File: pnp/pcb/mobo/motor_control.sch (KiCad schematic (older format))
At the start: 43 parts, among them J1 X_MOTOR, J2 Y_MOTOR1, J3 Z_MOTOR, J37 P_MOTOR, J38 C_MOTOR, J4 R_MOTOR, J48 Y_MOTOR2

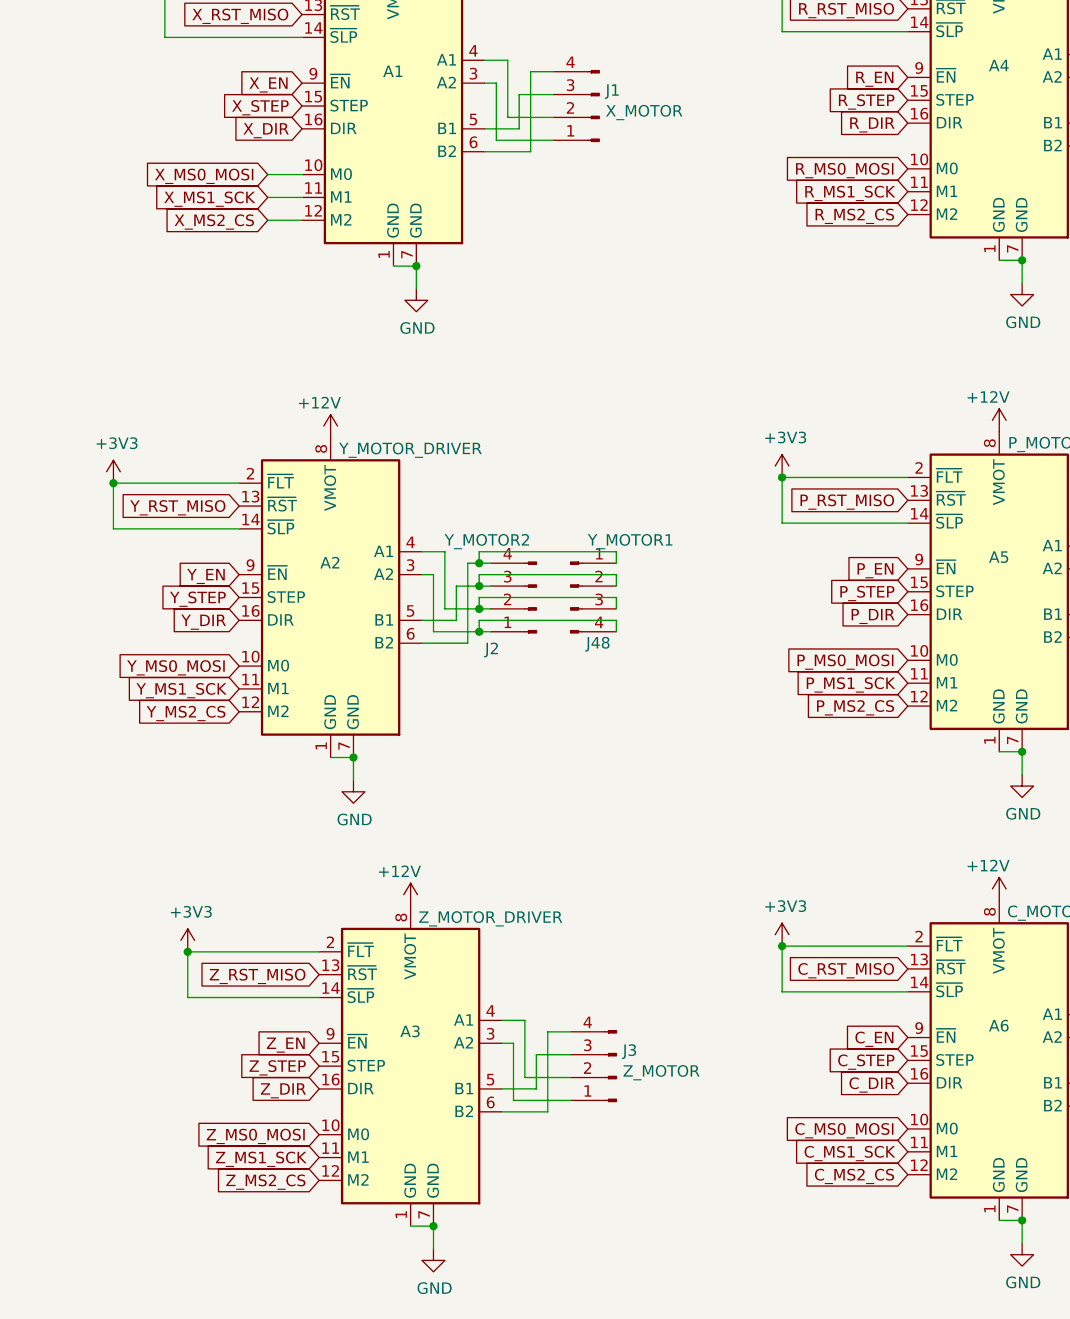
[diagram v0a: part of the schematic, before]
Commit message: Add support for Trinamic UART and SPI drivers
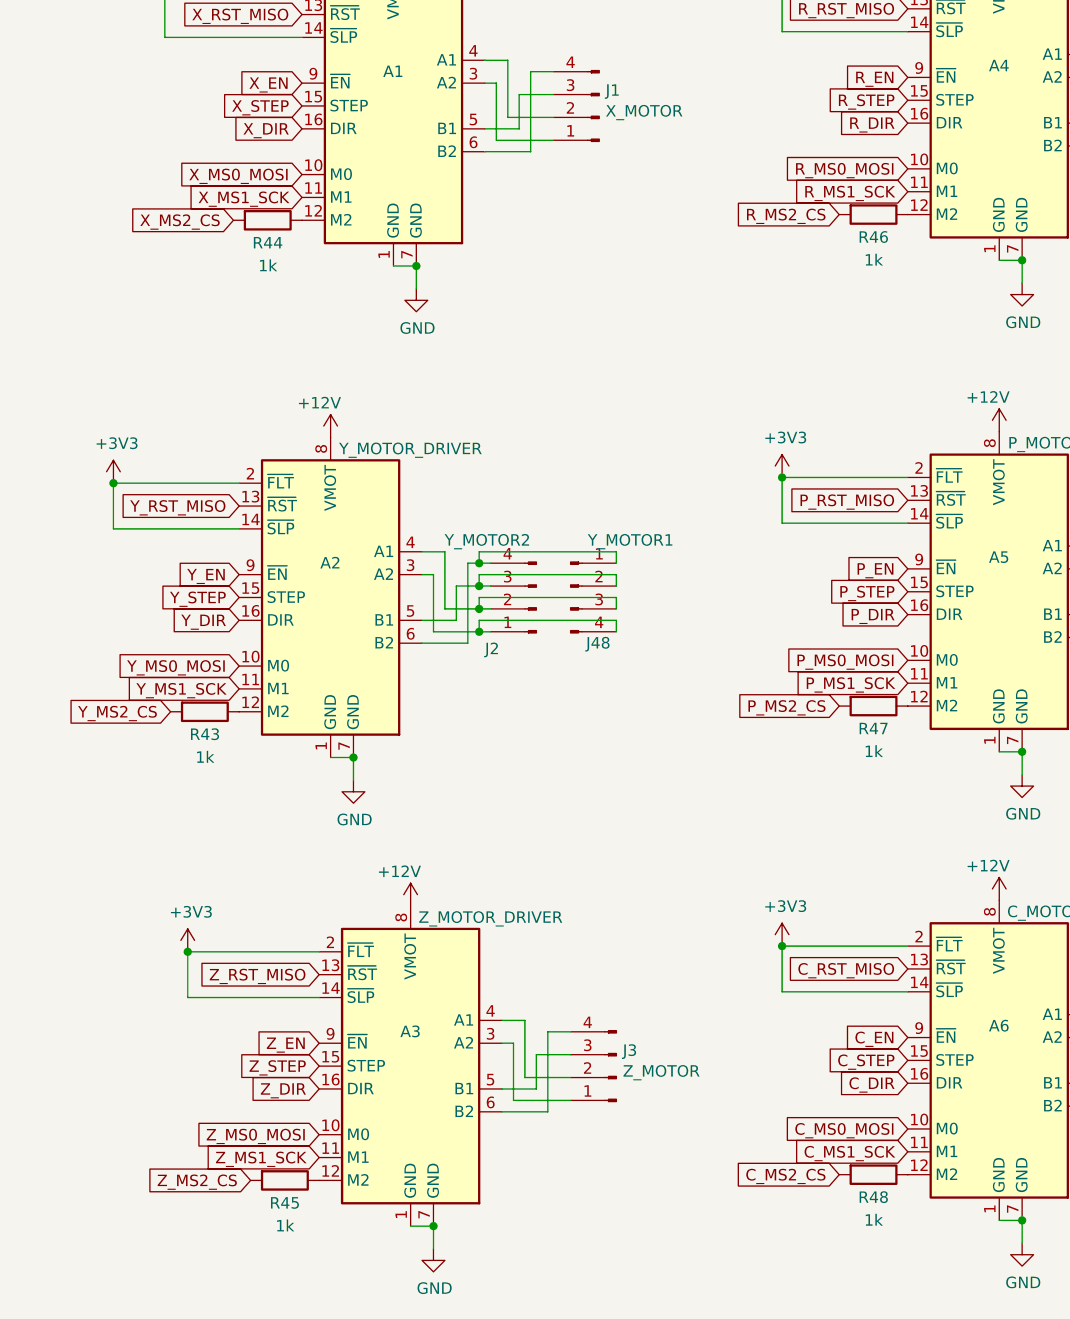
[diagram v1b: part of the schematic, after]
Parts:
- added R43, R44, R45, R46, R47, R48: 1k, Resistor_SMD:R_0805_2012Metric_Pad1.20x1.40mm_HandSolder, symbol Device:R
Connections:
- net C_MS2_CS: now also R48.2; no longer A6.12 (M2)
- net P_MS2_CS: now also R47.2; no longer A5.12 (M2)
- net R_MS2_CS: now also R46.2; no longer A4.12 (M2)
- net X_MS2_CS: now also R44.2; no longer A1.12 (M2)
- net Y_MS2_CS: now also R43.2; no longer A2.12 (M2)
- net Z_MS2_CS: now also R45.2; no longer A3.12 (M2)
- new net: A3.12 (M2), R45.1
- new net: A1.12 (M2), R44.1
- new net: A2.12 (M2), R43.1
- new net: A6.12 (M2), R48.1
- new net: A4.12 (M2), R46.1
- new net: A5.12 (M2), R47.1
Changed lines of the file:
@@
 Connection ~ 3050 1050
 Connection ~ 2650 1050
-Text GLabel 1825 2150 0    50   Input ~ 0
-X_EN
 Text GLabel 1825 2250 0    50   Input ~ 0
 X_STEP
@@
 Text GLabel 4475 2325 0    50   Input ~ 0
 R_DIR
-Text GLabel 1550 4300 0    50   Input ~ 0
-Y_EN
 Text GLabel 1550 4400 0    50   Input ~ 0
 Y_STEP
@@
 Text GLabel 4475 4475 0    50   Input ~ 0
 P_DIR
-Text GLabel 1900 6350 0    50   Input ~ 0
-Z_EN
 Text GLabel 1900 6450 0    50   Input ~ 0
 Z_STEP
@@
 Wire Wire Line
 	5275 2025 5375 2025
-Text GLabel 1675 2550 0    50   Input ~ 0
+Text GLabel 1825 2550 0    50   Input ~ 0
 X_MS0_MOSI
-Wire Wire Line
-	1675 2550 1825 2550
-Text GLabel 1675 2650 0    50   Input ~ 0
+Text GLabel 1825 2650 0    50   Input ~ 0
 X_MS1_SCK
-Text GLabel 1675 2750 0    50   Input ~ 0
+Text GLabel 1525 2750 0    50   Input ~ 0
 X_MS2_CS
 Text GLabel 1825 1850 0    50   Input ~ 0
@@
 	1225 1950 1825 1950
 Connection ~ 1225 1750
-Wire Wire Line
-	1675 2650 1825 2650
-Wire Wire Line
-	1675 2750 1825 2750
 Text GLabel 1550 4000 0    50   Input ~ 0
 Y_RST_MISO
@@
 Text GLabel 1550 4800 0    50   Input ~ 0
 Y_MS1_SCK
-Text GLabel 1550 4900 0    50   Input ~ 0
+Text GLabel 1250 4900 0    50   Input ~ 0
 Y_MS2_CS
 Wire Wire Line
@@
 Text GLabel 1900 6850 0    50   Input ~ 0
 Z_MS1_SCK
-Text GLabel 1900 6950 0    50   Input ~ 0
+Text GLabel 1600 6950 0    50   Input ~ 0
 Z_MS2_CS
 Text GLabel 4475 2525 0    50   Input ~ 0
@@
 Text GLabel 4475 2625 0    50   Input ~ 0
 R_MS1_SCK
-Text GLabel 4475 2725 0    50   Input ~ 0
+Text GLabel 4175 2725 0    50   Input ~ 0
 R_MS2_CS
 Text GLabel 4475 1825 0    50   Input ~ 0
@@
 Text GLabel 4475 4775 0    50   Input ~ 0
 P_MS1_SCK
-Text GLabel 4475 4875 0    50   Input ~ 0
+Text GLabel 4175 4875 0    50   Input ~ 0
 P_MS2_CS
 Text GLabel 4475 3975 0    50   Input ~ 0
@@
 Text GLabel 4475 6825 0    50   Input ~ 0
 C_MS1_SCK
-Text GLabel 4475 6925 0    50   Input ~ 0
+Text GLabel 4175 6925 0    50   Input ~ 0
 C_MS2_CS
 Text GLabel 4475 6025 0    50   Input ~ 0
@@
 	9300 1450 9300 1350
 Connection ~ 9300 1450
+Text GLabel 1825 2150 0    50   Input ~ 0
+X_EN
+Text GLabel 1900 6350 0    50   Input ~ 0
+Z_EN
+Text GLabel 1550 4300 0    50   Input ~ 0
+Y_EN
+$Comp
+L Device:R R47
+U 1 1 5FE64F8F
+P 4325 4875
+F 0 "R47" V 4425 4875 50  0000 C CNN
+F 1 "1k" V 4525 4875 50  0000 C CNN
+F 2 "Resistor_SMD:R_0805_2012Metric_Pad1.20x1.40mm_HandSolder" V 4255 4875 50  0001 C CNN
+F 3 "~" H 4325 4875 50  0001 C CNN
+	1    4325 4875
+	0    1    1    0
+$EndComp
+$Comp
+L Device:R R43
+U 1 1 5FE77D44
+P 1400 4900
+F 0 "R43" V 1500 4900 50  0000 C CNN
+F 1 "1k" V 1600 4900 50  0000 C CNN
+F 2 "Resistor_SMD:R_0805_2012Metric_Pad1.20x1.40mm_HandSolder" V 1330 4900 50  0001 C CNN
+F 3 "~" H 1400 4900 50  0001 C CNN
+	1    1400 4900
+	0    1    1    0
+$EndComp
+$Comp
+L Device:R R46
+U 1 1 5FE853A1
+P 4325 2725
+F 0 "R46" V 4425 2725 50  0000 C CNN
+F 1 "1k" V 4525 2725 50  0000 C CNN
+F 2 "Resistor_SMD:R_0805_2012Metric_Pad1.20x1.40mm_HandSolder" V 4255 2725 50  0001 C CNN
+F 3 "~" H 4325 2725 50  0001 C CNN
+	1    4325 2725
+	0    1    1    0
+$EndComp
+$Comp
+L Device:R R44
+U 1 1 5FE9EC8A
+P 1675 2750
+F 0 "R44" V 1775 2750 50  0000 C CNN
+F 1 "1k" V 1875 2750 50  0000 C CNN
+F 2 "Resistor_SMD:R_0805_2012Metric_Pad1.20x1.40mm_HandSolder" V 1605 2750 50  0001 C CNN
+F 3 "~" H 1675 2750 50  0001 C CNN
+	1    1675 2750
+	0    1    1    0
+$EndComp
+$Comp
+L Device:R R45
+U 1 1 5FEA6A5A
+P 1750 6950
+F 0 "R45" V 1850 6950 50  0000 C CNN
+F 1 "1k" V 1950 6950 50  0000 C CNN
+F 2 "Resistor_SMD:R_0805_2012Metric_Pad1.20x1.40mm_HandSolder" V 1680 6950 50  0001 C CNN
+F 3 "~" H 1750 6950 50  0001 C CNN
+	1    1750 6950
+	0    1    1    0
+$EndComp
+$Comp
+L Device:R R48
+U 1 1 5FEA9C63
+P 4325 6925
+F 0 "R48" V 4425 6925 50  0000 C CNN
+F 1 "1k" V 4525 6925 50  0000 C CNN
+F 2 "Resistor_SMD:R_0805_2012Metric_Pad1.20x1.40mm_HandSolder" V 4255 6925 50  0001 C CNN
+F 3 "~" H 4325 6925 50  0001 C CNN
+	1    4325 6925
+	0    1    1    0
+$EndComp
 $EndSCHEMATC

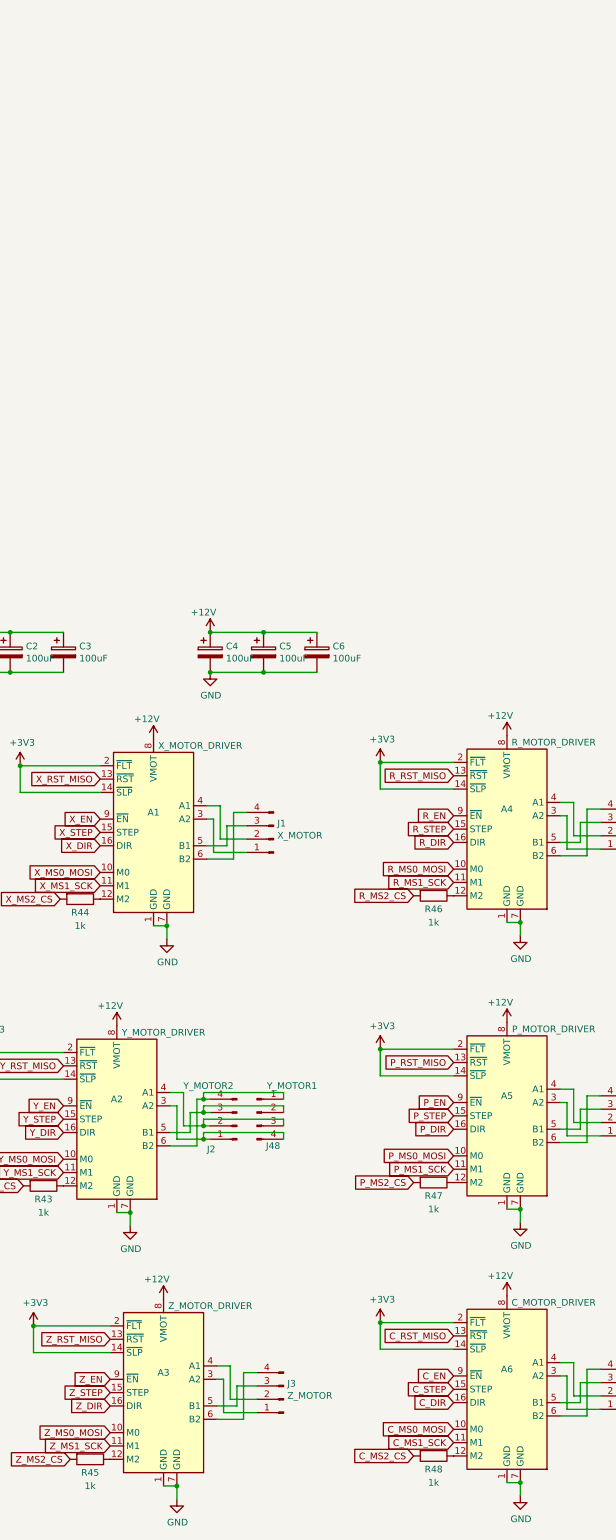
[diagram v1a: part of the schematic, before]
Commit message: Add 24VDC support
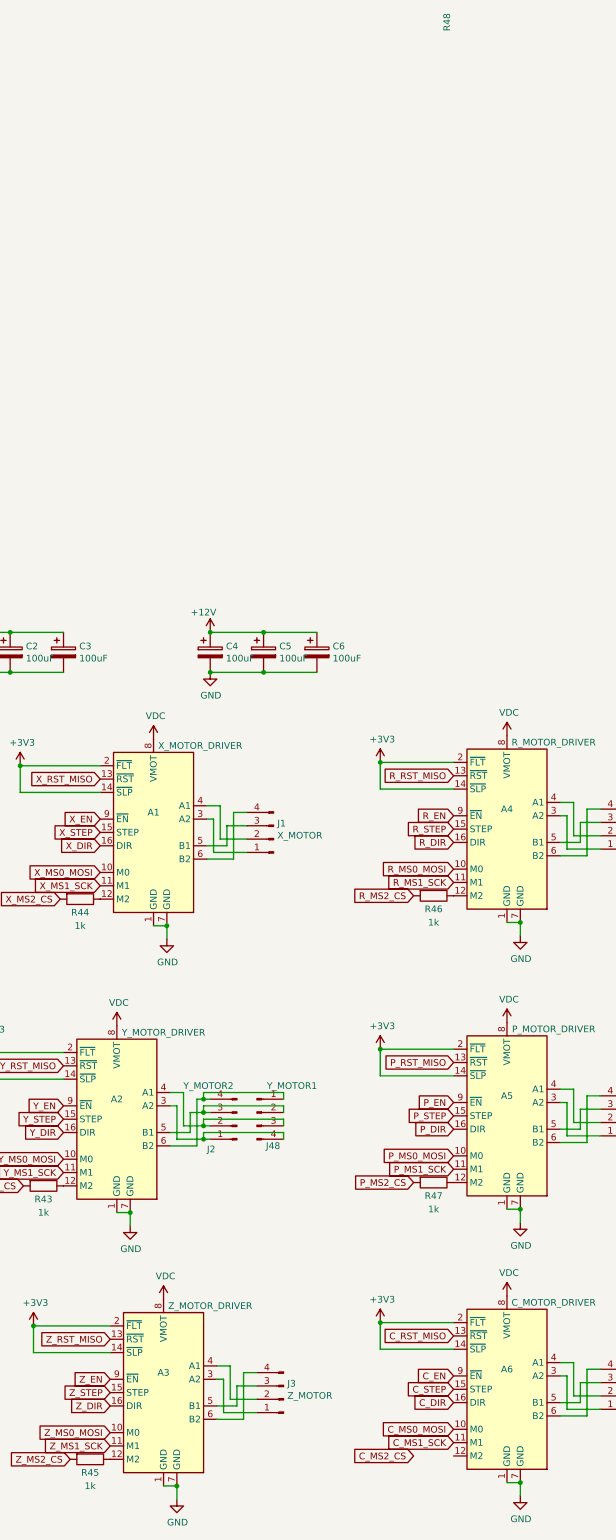
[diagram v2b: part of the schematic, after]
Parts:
- removed R48: 1k, Resistor_SMD:R_0805_2012Metric_Pad1.20x1.40mm_HandSolder, symbol Device:R
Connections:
- net +12V: no longer A1.8 (VMOT), A2.8 (VMOT), A3.8 (VMOT), A4.8 (VMOT), A5.8 (VMOT), A6.8 (VMOT)
- new net VDC: A1.8 (VMOT), A2.8 (VMOT), A3.8 (VMOT), A4.8 (VMOT), A5.8 (VMOT), A6.8 (VMOT)
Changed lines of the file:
@@
 Connection ~ 2400 7150
-$Comp
-L power:+12V #PWR0102
-U 1 1 5E406339
-P 2300 5750
-F 0 "#PWR0102" H 2300 5600 50  0001 C CNN
-F 1 "+12V" H 2250 5900 50  0000 C CNN
-F 2 "" H 2300 5750 50  0001 C CNN
-F 3 "" H 2300 5750 50  0001 C CNN
-	1    2300 5750
-	1    0    0    -1
-$EndComp
 $Comp
 L Connector:Conn_01x04_Male J3
@@
 	2325 2950 2225 2950
 $Comp
-L power:+12V #PWR0104
-U 1 1 5E418FAD
-P 2225 1550
-F 0 "#PWR0104" H 2225 1400 50  0001 C CNN
-F 1 "+12V" H 2175 1700 50  0000 C CNN
-F 2 "" H 2225 1550 50  0001 C CNN
-F 3 "" H 2225 1550 50  0001 C CNN
-	1    2225 1550
-	1    0    0    -1
-$EndComp
-$Comp
 L Connector:Conn_01x04_Male J1
 U 1 1 5E418FC1
@@
 	2050 5100 1950 5100
 $Comp
-L power:+12V #PWR0106
-U 1 1 5E421DF1
-P 1950 3700
-F 0 "#PWR0106" H 1950 3550 50  0001 C CNN
-F 1 "+12V" H 1900 3850 50  0000 C CNN
-F 2 "" H 1950 3700 50  0001 C CNN
-F 3 "" H 1950 3700 50  0001 C CNN
-	1    1950 3700
-	1    0    0    -1
-$EndComp
-$Comp
 L power:GND #PWR0108
 U 1 1 5E427C6A
@@
 	4975 7125 4875 7125
 Connection ~ 4975 7125
-$Comp
-L power:+12V #PWR0199
-U 1 1 5EB0D858
-P 4875 5725
-F 0 "#PWR0199" H 4875 5575 50  0001 C CNN
-F 1 "+12V" H 4825 5875 50  0000 C CNN
-F 2 "" H 4875 5725 50  0001 C CNN
-F 3 "" H 4875 5725 50  0001 C CNN
-	1    4875 5725
-	1    0    0    -1
-$EndComp
 $Comp
 L Connector:Conn_01x04_Male J38
@@
 	4975 2925 4875 2925
 $Comp
-L power:+12V #PWR0203
-U 1 1 5EB0D8B4
-P 4875 1525
-F 0 "#PWR0203" H 4875 1375 50  0001 C CNN
-F 1 "+12V" H 4825 1675 50  0000 C CNN
-F 2 "" H 4875 1525 50  0001 C CNN
-F 3 "" H 4875 1525 50  0001 C CNN
-	1    4875 1525
-	1    0    0    -1
-$EndComp
-$Comp
 L Connector:Conn_01x04_Male J4
 U 1 1 5EB0D8C8
@@
 Wire Wire Line
 	4975 5075 4875 5075
-$Comp
-L power:+12V #PWR0205
-U 1 1 5EB0D910
-P 4875 3675
-F 0 "#PWR0205" H 4875 3525 50  0001 C CNN
-F 1 "+12V" H 4825 3825 50  0000 C CNN
-F 2 "" H 4875 3675 50  0001 C CNN
-F 3 "" H 4875 3675 50  0001 C CNN
-	1    4875 3675
-	1    0    0    -1
-$EndComp
 $Comp
 L Connector:Conn_01x04_Male J37
@@
 	1    4325 6925
 	0    1    1    0
+$Comp
+L power:VDC #PWR03
+U 1 1 5FE11833
+P 2225 1550
+F 0 "#PWR03" H 2225 1450 50  0001 C CNN
+F 1 "VDC" H 2240 1723 50  0000 C CNN
+F 2 "" H 2225 1550 50  0001 C CNN
+F 3 "" H 2225 1550 50  0001 C CNN
+	1    2225 1550
+	1    0    0    -1
+$EndComp
+$Comp
+L power:VDC #PWR06
+U 1 1 5FE12359
+P 4875 1525
+F 0 "#PWR06" H 4875 1425 50  0001 C CNN
+F 1 "VDC" H 4890 1698 50  0000 C CNN
+F 2 "" H 4875 1525 50  0001 C CNN
+F 3 "" H 4875 1525 50  0001 C CNN
+	1    4875 1525
+	1    0    0    -1
+$EndComp
+$Comp
+L power:VDC #PWR07
+U 1 1 5FE163D9
+P 4875 3675
+F 0 "#PWR07" H 4875 3575 50  0001 C CNN
+F 1 "VDC" H 4890 3848 50  0000 C CNN
+F 2 "" H 4875 3675 50  0001 C CNN
+F 3 "" H 4875 3675 50  0001 C CNN
+	1    4875 3675
+	1    0    0    -1
+$EndComp
+$Comp
+L power:VDC #PWR08
+U 1 1 5FE16DA3
+P 4875 5725
+F 0 "#PWR08" H 4875 5625 50  0001 C CNN
+F 1 "VDC" H 4890 5898 50  0000 C CNN
+F 2 "" H 4875 5725 50  0001 C CNN
+F 3 "" H 4875 5725 50  0001 C CNN
+	1    4875 5725
+	1    0    0    -1
+$EndComp
+$Comp
+L power:VDC #PWR05
+U 1 1 5FE1767F
+P 2300 5750
+F 0 "#PWR05" H 2300 5650 50  0001 C CNN
+F 1 "VDC" H 2315 5923 50  0000 C CNN
+F 2 "" H 2300 5750 50  0001 C CNN
+F 3 "" H 2300 5750 50  0001 C CNN
+	1    2300 5750
+	1    0    0    -1
+$EndComp
+$Comp
+L power:VDC #PWR01
+U 1 1 5FE1815F
+P 1950 3700
+F 0 "#PWR01" H 1950 3600 50  0001 C CNN
+F 1 "VDC" H 1965 3873 50  0000 C CNN
+F 2 "" H 1950 3700 50  0001 C CNN
+F 3 "" H 1950 3700 50  0001 C CNN
+	1    1950 3700
+	1    0    0    -1
 $EndComp
 $EndSCHEMATC
